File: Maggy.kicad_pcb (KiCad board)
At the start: 2 copper layers, 160 x 100 mm, 125 parts, among them J1 XY308-2.54-2P, J2 XY308-2.54-2P, J3 XY308-2.54-2P, J4 XY308-2.54-2P, U1 CH224K, U10 INA214AIDCKR, U11 Socket for Teensy 4.1 (2x 1x2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, U12 INA214AIDCKR, U13 INA214AIDCKR, U14 TMAG5170A2DGKR, U15 TMAG5170A2DGKR, U16 TMAG5170A2DGKR, U17 TMAG5170A2DGKR, U18 TMAG5170A2DGKR, U2 A4950ELJTR-T, U3 A4950ELJTR-T, U4 A4950ELJTR-T, U5 A4950ELJTR-T, U6 TLV2372, U7 LM1117S-3.3, U8 LM1117S-5.0, U9 INA214AIDCKR

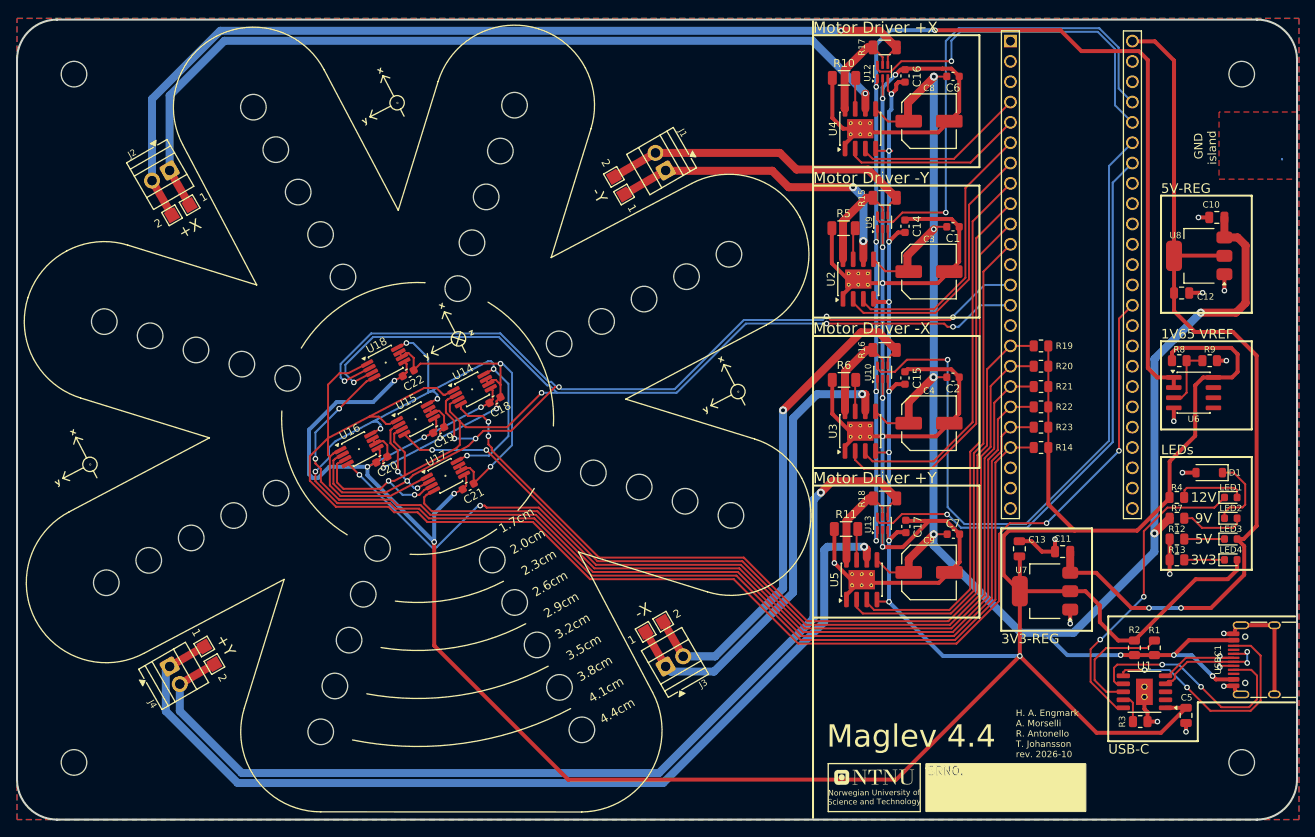
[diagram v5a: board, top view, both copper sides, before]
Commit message: chore: add test points for power, fix ground island so it is accessible on back as well
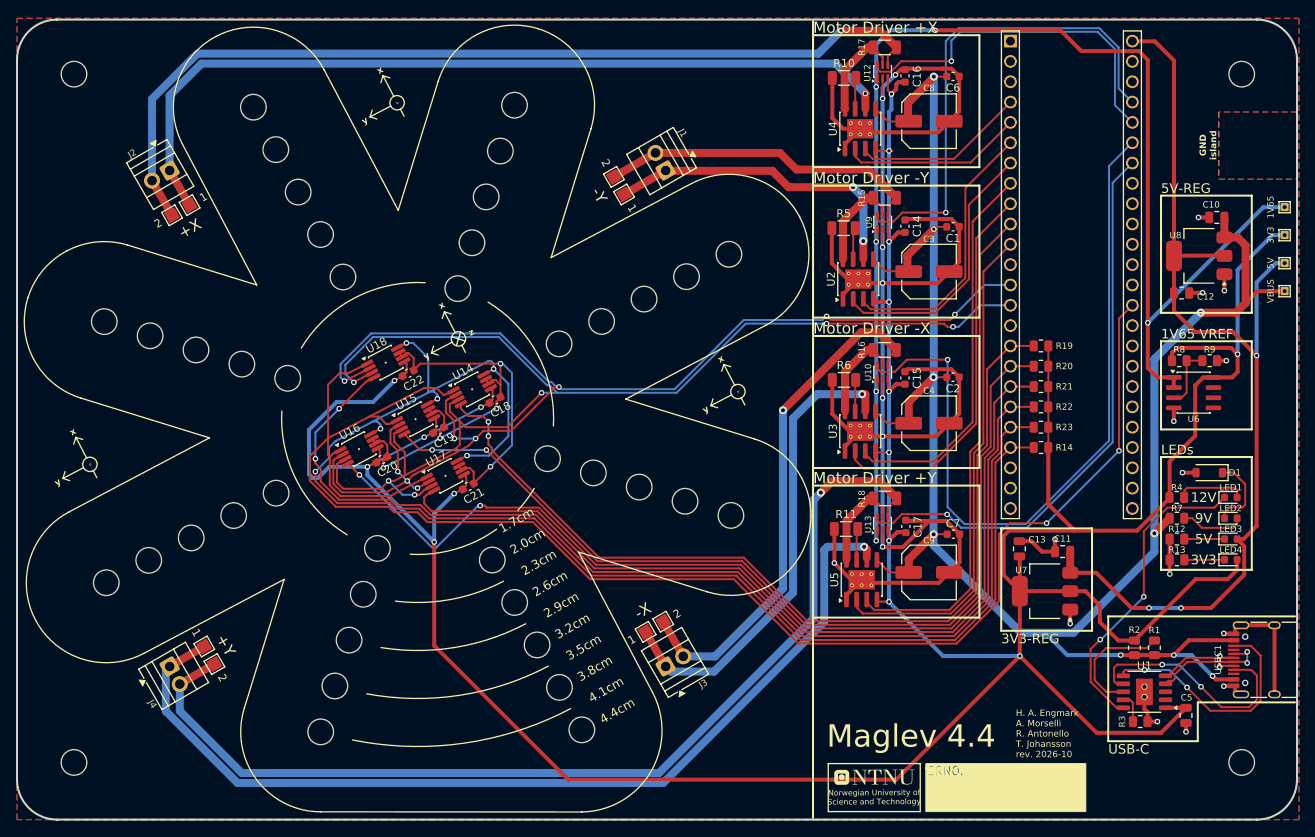
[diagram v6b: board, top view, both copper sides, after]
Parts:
- added 1V65: TestPoint_THTPad_1.0x1.0mm_Drill0.5mm, TestPoint:TestPoint_THTPad_1.0x1.0mm_Drill0.5mm, F.Cu at (228.4, 83.5)
- added 3V3: TestPoint_THTPad_1.0x1.0mm_Drill0.5mm, TestPoint:TestPoint_THTPad_1.0x1.0mm_Drill0.5mm, F.Cu at (228.4, 87.0)
- added 5V: TestPoint_THTPad_1.0x1.0mm_Drill0.5mm, TestPoint:TestPoint_THTPad_1.0x1.0mm_Drill0.5mm, F.Cu at (228.4, 90.5)
- added VBUS: TestPoint_THTPad_1.0x1.0mm_Drill0.5mm, TestPoint:TestPoint_THTPad_1.0x1.0mm_Drill0.5mm, F.Cu at (228.4, 94.0)
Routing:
- net +1V65: track 148.2 -> 171.3 mm, vias 5 -> 6
- net +3V3: track 452.6 -> 470.8 mm, vias 15 -> 16
- net +5V: track 113.8 -> 127.4 mm, vias 2 -> 3
- net VBUS: track 235.9 -> 241.4 mm
- net 2_1: track 108.9 -> 106.5 mm
